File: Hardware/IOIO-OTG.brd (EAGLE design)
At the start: 68.6 x 30.5 mm, 53 parts, among them Q1 IRLML2244, Q2 2N7002PW, U1 PIC24FJ256GB206, U14 SWITCH_SPDT, U2 TPS62133RGTT, U3 VREG_MIC5216

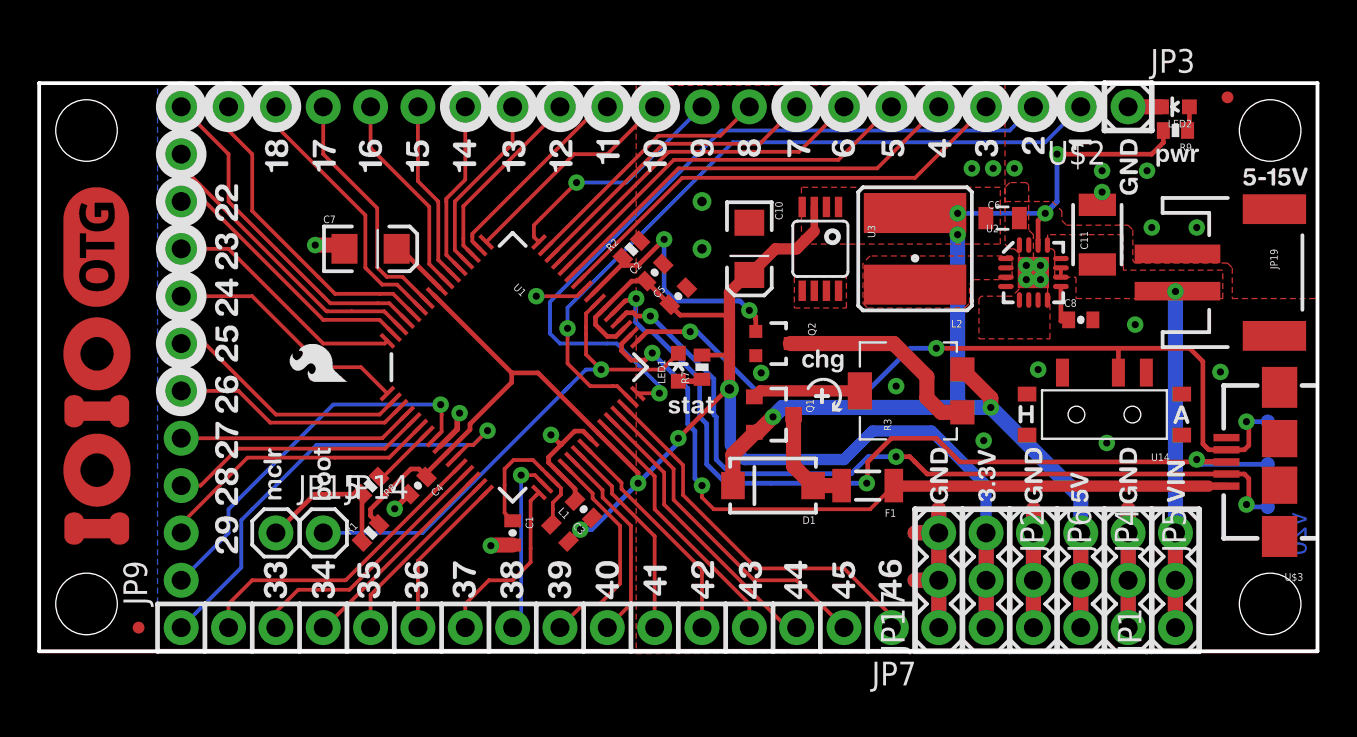
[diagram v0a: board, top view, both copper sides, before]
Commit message: Heavy Revision
(1) Created and added a new 1:1 FP for the TPS... IC
(2) Routed all traces directly out from the TPS... IC
(3) 0402 --> 0603
(4) Created and added a new FP for a new microAB USB connector, this new
FP is based off of the data-sheet for the new USB microAB that should
have guiding bosses (very much trial right now).
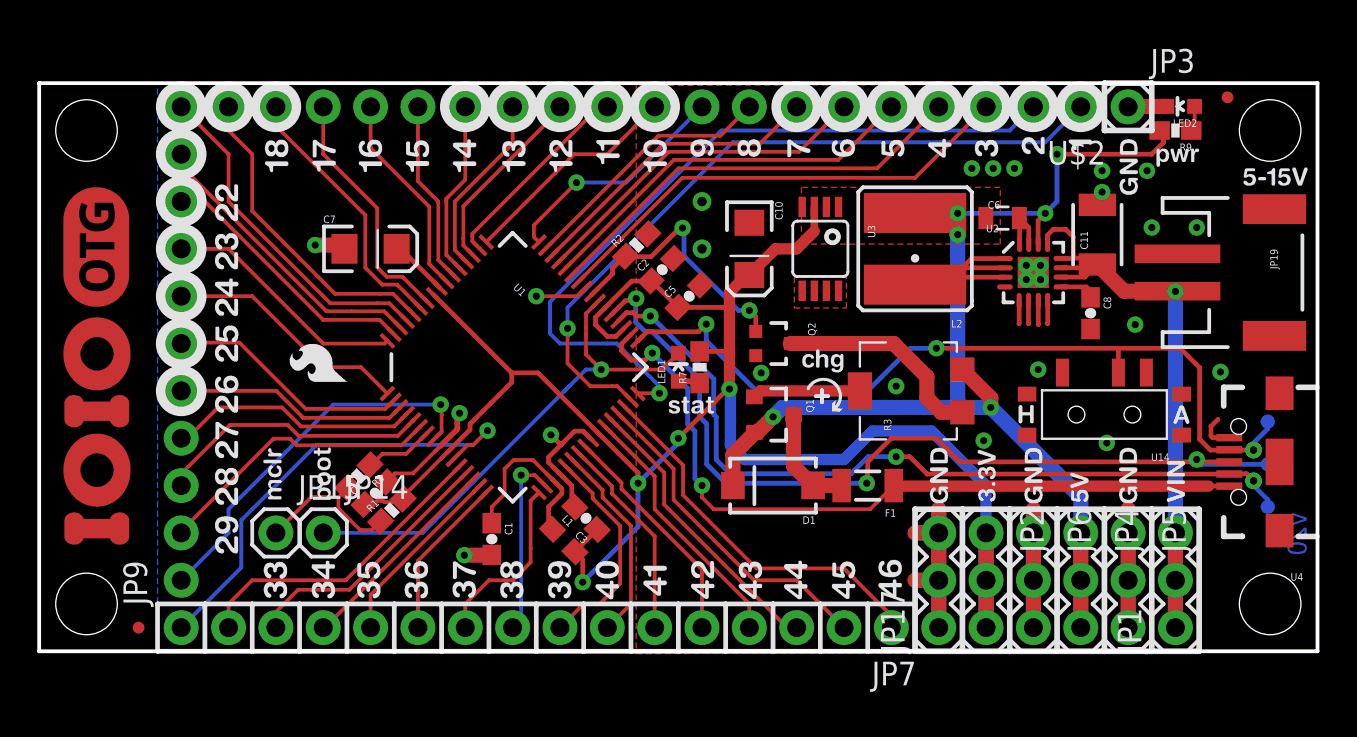
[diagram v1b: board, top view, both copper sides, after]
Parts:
- removed U$3: 10104111-0001LF, SparkFun-Connectors:USB-AB-MICRO-SMD
- added U4: (no value), Testing:USB-AB-MICRO-SMD_V02_BOSS
- C1, C2, C3, C4, C5, C8: device SparkFun:0402-CAP -> SparkFun-Capacitors:0603-CAP
- L1: device SparkFun-Passives:C0402 -> SparkFun-Passives:0603
- LED1: device SparkFun:LED-0603 -> SparkFun-LED:LED-0603
- R1, R2, R7, R8, R9: device SparkFun:0402-RES -> SparkFun-Resistors:0603-RES
- U2: value TPS62133RGTT -> TPS6214X""; device SparkFun-PowerIC:QFN16-3X3MM -> SparkFun-PowerIC:QFN16-3X3MM_1:1_V03
- moved C4 2.32 mm to (18.0, 8.48), turned to 45 degrees
- moved R1 1.67 mm to (18.9, 7.57)
- moved C1 1.17 mm to (24.3, 6.02)
- moved R8 0.81 mm to (17.1, 9.40)
- moved C8 0.64 mm to (56.4, 18.1), turned to 270 degrees
- moved C5 0.58 mm to (34.9, 19.1)
- moved C3 0.50 mm to (29.3, 7.14)
- moved L1 0.45 mm to (28.1, 5.94)
- moved C2 0.43 mm to (33.4, 20.5)
- moved R2 0.36 mm to (32.1, 21.8)
- moved LED2 0.28 mm to (61.2, 29.2)
- moved R7 0.13 mm to (35.4, 15.2)
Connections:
- net D+: now also U4.D+1; no longer U$3.D+
- net D-: now also U4.D-1; no longer U$3.D-
- net GND: now also U4.GND1; no longer U$3.GND
- net USBID: now also U4.ID1; no longer U$3.ID
- net VBUS: now also U4.VBUS1; no longer U$3.VBUS
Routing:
- net GND: track 60.7 -> 74.3 mm, vias 27 -> 26
- net VIN: track 26.2 -> 37.6 mm
- net N$6: track 0.00 -> 10.5 mm
- net 3.3V: track 98.1 -> 101.7 mm
- net D+: track 48.4 -> 47.0 mm
- net PIN28: track 13.9 -> 14.8 mm
- net PIN27: track 12.7 -> 13.6 mm
- net 5V: track 66.3 -> 65.4 mm
- net N$9: track 8.96 -> 9.66 mm
- net D-: track 43.6 -> 43.0 mm
- net P7: track 8.02 -> 8.55 mm
- removed copper zone on layer 1, net N$6
- removed copper zone on layer 1, net VIN

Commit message: More changes:
-removed test-points from below the microAB
-Moved "PWR" LED and RES out just a bit more to clear headers on the OTG
w/ Headers
-Created and added a new TRIMPOT FP per Bob's request
-Added T-Stop around the PIC to allow Tyler T. to be able to inspect the
PIC with the AOI
-Also added a new new microAB FP
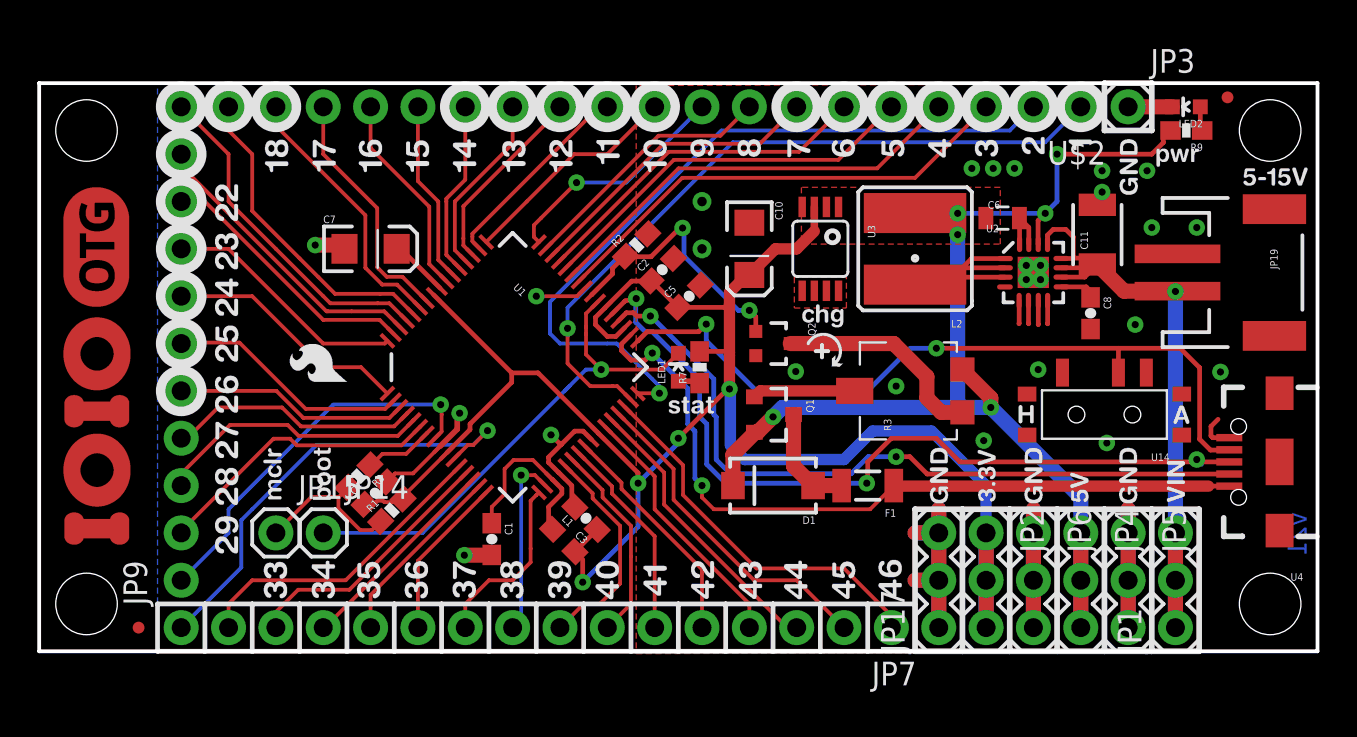
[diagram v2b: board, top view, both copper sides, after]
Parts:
- removed TP1, TP2, TP3: TEST-POINT3, SparkFun-Passives:PAD.03X.03
- R3: device SparkFun-Electromechanical:TRIMPOT-5MM -> Testing:TRIMPOT_5MM
- U4: device Testing:USB-AB-MICRO-SMD_V02_BOSS -> Testing:USB-AB-MICRO-SMD_V03
- moved R9 0.58 mm to (61.5, 27.9)
- moved LED2 0.31 mm to (61.5, 29.2)
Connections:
- net D+: no longer TP2.P$1
- net D-: no longer TP3.P$1
- net USBID: no longer TP1.P$1
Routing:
- net D+: track 47.0 -> 43.4 mm
- net D-: track 43.0 -> 39.8 mm, vias 3 -> 2
- net USBID: track 44.0 -> 40.9 mm, vias 3 -> 2
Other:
- board text added: "v21"
- board text removed: "v20"
